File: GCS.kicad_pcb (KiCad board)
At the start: 2 copper layers, 0 parts

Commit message: Added redesigned schematics, missing EEPROM
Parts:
- added C1: 15nF, Capacitor_THT:C_Rect_L7.0mm_W3.5mm_P5.00mm, F.Cu at (104.1, 86.4)
- added C10: 100nF, Capacitor_THT:C_Rect_L7.0mm_W3.5mm_P5.00mm, F.Cu at (97.9, 143.5)
- added C11: 100nF, Capacitor_THT:C_Rect_L7.0mm_W3.5mm_P5.00mm, F.Cu at (54.6, 179.1)
- added C2: 100nF, Capacitor_THT:C_Rect_L7.0mm_W3.5mm_P5.00mm, F.Cu at (110.2, -12.9)
- added C3: 15nF, Capacitor_THT:C_Rect_L7.0mm_W3.5mm_P5.00mm, F.Cu at (104.1, 91.4)
- added C4: 100nF, Capacitor_THT:C_Rect_L7.0mm_W3.5mm_P5.00mm, F.Cu at (101.6, -18.0)
- added C5: 100nF, Capacitor_THT:C_Rect_L7.0mm_W3.5mm_P5.00mm, F.Cu at (110.2, -18.0)
- added C6: 100nF, Capacitor_THT:C_Rect_L7.0mm_W3.5mm_P5.00mm, F.Cu at (118.7, -18.0)
- added C7: 100nF, Capacitor_THT:C_Rect_L7.0mm_W3.5mm_P5.00mm, F.Cu at (101.6, -12.9)
- added C8: 100nF, Capacitor_THT:C_Rect_L7.0mm_W3.5mm_P5.00mm, F.Cu at (87.6, 81.2)
- added C9: 100nF, Capacitor_THT:C_Rect_L7.0mm_W3.5mm_P5.00mm, F.Cu at (63.5, 88.8)
- added J1: Conn_01x02_Male, Connector_PinHeader_1.00mm:PinHeader_1x02_P1.00mm_Vertical, F.Cu at (108.0, 78.7)
- added J2: USB_B, Connector_USB:USB_B_OST_USB-B1HSxx_Horizontal, F.Cu at (33.0, -2.54)
- added J3: Conn_01x04_Male, Connector_PinHeader_1.00mm:PinHeader_1x04_P1.00mm_Vertical, F.Cu at (171.5, -65.6)
- added J4: Conn_02x03_Counter_Clockwise, Connector_PinHeader_1.00mm:PinHeader_2x03_P1.00mm_Vertical, F.Cu at (127.2, -12.2)
- added J5: Conn_01x04_Male, Connector_PinHeader_1.00mm:PinHeader_1x04_P1.00mm_Vertical, F.Cu at (174.8, -65.6)
- added J6: Conn_02x03_Counter_Clockwise, Connector_PinHeader_1.00mm:PinHeader_2x03_P1.00mm_Vertical, F.Cu at (171.5, -59.5)
- added SW1: SW_Push, Button_Switch_THT:SW_PUSH_6mm, F.Cu at (99.1, 80.0)
- added U1: MC6809, Package_DIP:DIP-40_W15.24mm_Socket, F.Cu at (77.5, 85.1)
- added U10: 74HCT00, Package_DIP:DIP-14_W7.62mm_Socket, F.Cu at (48.3, 160.0)
- added U2: DS1813, Package_TO_SOT_THT:TO-92_Inline, F.Cu at (111.8, 97.8)
- added U3: MC68B21, Package_DIP:DIP-40_W15.24mm, F.Cu at (111.9, -70.8)
- added U4: HM62256BLP-7, Package_DIP:DIP-28_W15.24mm_Socket, F.Cu at (73.7, 125.7)
- added U5: 74LS138, Package_DIP:DIP-16_W7.62mm, F.Cu at (94.0, 137.2)
- added U6: 74LS138, Package_DIP:DIP-16_W7.62mm, F.Cu at (160.6, -70.8)
- added U7: 74LS138, Package_DIP:DIP-16_W7.62mm, F.Cu at (149.7, -70.8)
- added U8: MC6850, Package_DIP:DIP-40_W15.24mm, F.Cu at (93.5, -70.8)
- added U9: MC6850, Package_DIP:DIP-40_W15.24mm, F.Cu at (75.1, -70.8)
- added X1: ACO-xxxMHz, Oscillator:Oscillator_DIP-14, F.Cu at (106.7, 114.3)
- added Y1: Crystal, Crystal:Crystal_HC18-U_Vertical, F.Cu at (99.1, 86.4)
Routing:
- net GND: track 0.00 -> 93.3 mm
- net /A15: track 0.00 -> 82.0 mm
- net VCC: track 0.00 -> 72.0 mm
- net /A13: track 0.00 -> 70.4 mm
- net /A14: track 0.00 -> 50.5 mm
- net /~RESET: track 0.00 -> 49.4 mm
- net /D3: track 0.00 -> 44.7 mm
- net /A10: track 0.00 -> 43.4 mm
- net /A11: track 0.00 -> 42.4 mm
- net /D2: track 0.00 -> 35.4 mm
- net /A9: track 0.00 -> 31.3 mm
- net /XTAL: track 0.00 -> 29.5 mm
- net /D1: track 0.00 -> 29.3 mm
- net /EXTAL: track 0.00 -> 26.2 mm
- net /A8: track 0.00 -> 24.7 mm
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
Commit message: Added resistors on async io and changed IC footprints to sockets
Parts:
- added C12: 100nF, Capacitor_THT:C_Rect_L7.0mm_W3.5mm_P5.00mm, F.Cu at (83.4, 86.9)
- added R1: 2.7k, Resistor_THT:R_Axial_DIN0207_L6.3mm_D2.5mm_P7.62mm_Horizontal, F.Cu at (129.5, 23.5)
- added R10: 2.7k, Resistor_THT:R_Axial_DIN0207_L6.3mm_D2.5mm_P7.62mm_Horizontal, F.Cu at (95.8, 73.7)
- added R11: 2.7k, Resistor_THT:R_Axial_DIN0207_L6.3mm_D2.5mm_P7.62mm_Horizontal, F.Cu at (136.8, 31.6)
- added R12: 2.7k, Resistor_THT:R_Axial_DIN0207_L6.3mm_D2.5mm_P7.62mm_Horizontal, F.Cu at (126.0, 35.7)
- added R13: 2.7k, Resistor_THT:R_Axial_DIN0207_L6.3mm_D2.5mm_P7.62mm_Horizontal, F.Cu at (107.6, 58.2)
- added R14: 2.7k, Resistor_THT:R_Axial_DIN0207_L6.3mm_D2.5mm_P7.62mm_Horizontal, F.Cu at (126.0, 39.7)
- added R15: 2.7k, Resistor_THT:R_Axial_DIN0207_L6.3mm_D2.5mm_P7.62mm_Horizontal, F.Cu at (107.6, 54.2)
- added R16: 2.7k, Resistor_THT:R_Axial_DIN0207_L6.3mm_D2.5mm_P7.62mm_Horizontal, F.Cu at (53.5, 87.0)
- added R2: 2.7k, Resistor_THT:R_Axial_DIN0207_L6.3mm_D2.5mm_P7.62mm_Horizontal, F.Cu at (129.5, 27.6)
- added R3: 2.7k, Resistor_THT:R_Axial_DIN0207_L6.3mm_D2.5mm_P7.62mm_Horizontal, F.Cu at (115.2, 31.1)
- added R4: 2.7k, Resistor_THT:R_Axial_DIN0207_L6.3mm_D2.5mm_P7.62mm_Horizontal, F.Cu at (115.2, 35.2)
- added R5: 2.7k, Resistor_THT:R_Axial_DIN0207_L6.3mm_D2.5mm_P7.62mm_Horizontal, F.Cu at (115.2, 39.2)
- added R6: 2.7k, Resistor_THT:R_Axial_DIN0207_L6.3mm_D2.5mm_P7.62mm_Horizontal, F.Cu at (115.2, 43.3)
- added R7: 2.7k, Resistor_THT:R_Axial_DIN0207_L6.3mm_D2.5mm_P7.62mm_Horizontal, F.Cu at (115.2, 47.3)
- added R8: 2.7k, Resistor_THT:R_Axial_DIN0207_L6.3mm_D2.5mm_P7.62mm_Horizontal, F.Cu at (72.4, 86.4)
- added R9: 2.7k, Resistor_THT:R_Axial_DIN0207_L6.3mm_D2.5mm_P7.62mm_Horizontal, F.Cu at (126.0, 31.6)
- added U11: 74HCT00, Package_DIP:DIP-14_W7.62mm_Socket, F.Cu at (96.3, 54.3)
- J3, J5: value Conn_01x04_Male -> Conn_02x03_Counter_Clockwise; footprint Connector_PinHeader_1.00mm:PinHeader_1x04_P1.00mm_Vertical -> Connector_PinHeader_1.00mm:PinHeader_2x03_P1.00mm_Vertical
- J4, J6: value Conn_02x03_Counter_Clockwise -> Conn_01x04_Male; footprint Connector_PinHeader_1.00mm:PinHeader_2x03_P1.00mm_Vertical -> Connector_PinHeader_1.00mm:PinHeader_1x04_P1.00mm_Vertical
- U10: value 74HCT00 -> MC6850; footprint Package_DIP:DIP-14_W7.62mm_Socket -> Package_DIP:DIP-40_W15.24mm_Socket
- U3: footprint Package_DIP:DIP-40_W15.24mm -> Package_DIP:DIP-40_W15.24mm_Socket
- U5: value 74LS138 -> 29C256; footprint Package_DIP:DIP-16_W7.62mm -> Package_DIP:DIP-28_W15.24mm_Socket
- U6, U7: footprint Package_DIP:DIP-16_W7.62mm -> Package_DIP:DIP-16_W7.62mm_Socket
- U8: footprint Package_DIP:DIP-40_W15.24mm -> Package_DIP:DIP-24_W15.24mm_Socket
- U9: value MC6850 -> 74LS138; footprint Package_DIP:DIP-40_W15.24mm -> Package_DIP:DIP-16_W7.62mm_Socket
- X1: value ACO-xxxMHz -> CXO_DIP8; footprint Oscillator:Oscillator_DIP-14 -> Oscillator:Oscillator_DIP-8
- moved U7 184.1 mm to (30.5, 69.5)
- moved C11 184.1 mm to (142.6, 17.4), turned to 0 degrees
- moved U6 183.6 mm to (42.2, 69.5)
- moved J6 167.0 mm to (72.5, 74.9)
- moved J5 160.1 mm to (104.5, 78.2)
- moved U9 151.2 mm to (18.7, 69.5)
- moved U10 143.4 mm to (38.1, 17.0)
- moved U3 128.0 mm to (18.7, 17.0)
- moved U8 126.2 mm to (76.9, 54.3)
- moved U5 121.4 mm to (76.9, 17.0), turned to 0 degrees
- moved U4 111.1 mm to (96.3, 17.0), turned to 0 degrees
- moved J3 104.1 mm to (145.4, 35.2)
- moved C10 103.2 mm to (126.2, 44.3), turned to 0 degrees
- moved C5 102.2 mm to (96.0, 83.3)
- moved J4 97.8 mm to (72.5, 68.9)
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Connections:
- J2 pad 2: Net-(J2-Pad2) -> (no net)
- J2 pad 3: Net-(J2-Pad3) -> (no net)
- J3 pad 1: GND -> Net-(J3-Pad1)
- J3 pad 2: /TX0 -> Net-(J3-Pad2)
- J3 pad 3: /RX0 -> Net-(J3-Pad3)
- J3 pad 4: VCC -> GND
- J4 pad 1: /~DCD0 -> GND
- J4 pad 2: /~CTS0 -> Net-(J4-Pad2)
- J4 pad 3: /~RTS0 -> Net-(J4-Pad3)
- J4 pad 4: GND -> VCC
- J5 pad 1: GND -> Net-(J5-Pad1)
- J5 pad 2: /TX1 -> Net-(J5-Pad2)
- J5 pad 3: /RX1 -> Net-(J5-Pad3)
- J5 pad 4: VCC -> GND
- J6 pad 1: /~DCD1 -> GND
- J6 pad 2: /~CTS1 -> Net-(J6-Pad2)
- J6 pad 3: /~RTS1 -> Net-(J6-Pad3)
- J6 pad 4: GND -> VCC
- U1 pad 2: Net-(U1-Pad2) -> (no net)
- U1 pad 3: Net-(U1-Pad3) -> /~IRQ
- U1 pad 33: VCC -> Net-(R1-Pad2)
- U1 pad 35: Net-(U1-Pad35) -> (no net)
- U1 pad 36: VCC -> Net-(R1-Pad2)
- U1 pad 4: Net-(U1-Pad4) -> (no net)
- U1 pad 40: VCC -> Net-(R1-Pad2)
- U1 pad 5: Net-(U1-Pad5) -> (no net)
- U1 pad 6: Net-(U1-Pad6) -> (no net)
- U10 pad 1: /E -> GND
- U10 pad 10: /~R~W -> Net-(R11-Pad1)
- U10 pad 11: /BRAM -> /A0
- U10 pad 12: /~BRAM0 -> VCC
- U10 pad 13: /~BRAM1 -> /R~W
- U10 pad 14: VCC -> /E
- U10 pad 2: /R~W -> /RX1
- U10 pad 3: /~R -> /E
- U10 pad 4: /R~W -> /E
- U10 pad 5: /R~W -> /~RTS1
- U10 pad 6: /~R~W -> /TX1
- U10 pad 7: GND -> /~IRQ
- U10 pad 8: /~W -> Net-(R11-Pad1)
- U10 pad 9: /E -> /~ASYNC1_E
- U3 pad 10: Net-(U3-Pad10) -> (no net)
- U3 pad 11: Net-(U3-Pad11) -> (no net)
- U3 pad 12: Net-(U3-Pad12) -> (no net)
- U3 pad 13: Net-(U3-Pad13) -> (no net)
- U3 pad 14: Net-(U3-Pad14) -> (no net)
- U3 pad 15: Net-(U3-Pad15) -> (no net)
- U3 pad 16: Net-(U3-Pad16) -> (no net)
- U3 pad 17: Net-(U3-Pad17) -> (no net)
- U3 pad 18: Net-(U3-Pad18) -> (no net)
- U3 pad 19: Net-(U3-Pad19) -> (no net)
- U3 pad 2: Net-(U3-Pad2) -> (no net)
- U3 pad 22: VCC -> Net-(R2-Pad1)
- U3 pad 24: VCC -> Net-(R2-Pad1)
- U3 pad 3: Net-(U3-Pad3) -> (no net)
- U3 pad 37: Net-(U3-Pad37) -> /~IRQ
- U3 pad 38: Net-(U3-Pad38) -> /~IRQ
- U3 pad 39: Net-(U3-Pad39) -> (no net)
- U3 pad 4: Net-(U3-Pad4) -> (no net)
- U3 pad 40: Net-(U3-Pad40) -> (no net)
- U3 pad 5: Net-(U3-Pad5) -> (no net)
- U3 pad 6: Net-(U3-Pad6) -> (no net)
- U3 pad 7: Net-(U3-Pad7) -> (no net)
- U3 pad 8: Net-(U3-Pad8) -> (no net)
- U3 pad 9: Net-(U3-Pad9) -> (no net)
- U5 pad 1: /A13 -> /~W
- U5 pad 10: /~BRAM1 -> /A0
- U5 pad 11: /~BRAM0 -> /D0
- U5 pad 12: Net-(U5-Pad12) -> /D1
- U5 pad 13: Net-(U5-Pad13) -> /D2
- U5 pad 14: Net-(U5-Pad14) -> GND
- U5 pad 15: Net-(U5-Pad15) -> /D3
- U5 pad 16: VCC -> /D4
- U5 pad 2: /A14 -> /A12
- U5 pad 3: /A15 -> /A7
- U5 pad 4: GND -> /A6
- U5 pad 5: GND -> /A5
- U5 pad 6: /A15 -> /A4
- U5 pad 7: /~ROM -> /A3
- U5 pad 8: GND -> /A2
- U5 pad 9: /~IO -> /A1
- U6 pad 1: /A10 -> /A13
- U6 pad 10: /~IO5 -> /~BRAM1
- U6 pad 11: /~IO4 -> /~BRAM0
- U6 pad 12: /~IO3 -> (no net)
- U6 pad 13: /~IO2 -> (no net)
- U6 pad 14: /~IO1 -> (no net)
- U6 pad 15: /~INT_IO -> (no net)
- U6 pad 2: /A11 -> /A14
- U6 pad 3: /A12 -> /A15
- U6 pad 5: /~IO -> GND
- U6 pad 6: VCC -> /A15
- U6 pad 7: /~IO7 -> /~ROM
- U6 pad 9: /~IO6 -> /~IO
- U7 pad 1: /A4 -> /A10
- U7 pad 10: Net-(U7-Pad10) -> (no net)
- U7 pad 11: /~VDP_E -> (no net)
- U7 pad 12: /~ASYNC1_E -> (no net)
- U7 pad 13: /~ASYNC0_E -> (no net)
- U7 pad 14: /~PIA_E -> (no net)
- U7 pad 15: /~CFLASH_E -> /~INT_IO
- U7 pad 2: /A5 -> /A11
- U7 pad 3: /A6 -> /A12
- U7 pad 5: /~INT_IO -> /~IO
- U7 pad 6: VCC -> Net-(R3-Pad1)
- U7 pad 7: Net-(U7-Pad7) -> (no net)
- U7 pad 9: Net-(U7-Pad9) -> (no net)
- U8 pad 10: VCC -> Net-(R4-Pad1)
- U8 pad 15: Net-(U8-Pad15) -> (no net)
- U8 pad 16: Net-(U8-Pad16) -> (no net)
- U8 pad 17: Net-(U8-Pad17) -> (no net)
- U8 pad 18: Net-(U8-Pad18) -> (no net)
- U8 pad 19: Net-(U8-Pad19) -> (no net)
- U8 pad 20: Net-(U8-Pad20) -> (no net)
- U8 pad 21: Net-(U8-Pad21) -> (no net)
- U8 pad 22: Net-(U8-Pad22) -> (no net)
- U8 pad 7: Net-(U8-Pad7) -> /~IRQ
- U8 pad 8: VCC -> Net-(R4-Pad1)
- U9 pad 1: GND -> /A4
- U9 pad 10: VCC -> (no net)
- U9 pad 11: /A0 -> (no net)
- U9 pad 12: VCC -> /~ASYNC1_E
- U9 pad 13: /R~W -> /~ASYNC0_E
- U9 pad 14: /E -> /~PIA_E
- U9 pad 15: Net-(U9-Pad15) -> (no net)
- U9 pad 16: Net-(U9-Pad16) -> VCC
- U9 pad 2: /RX1 -> /A5
- U9 pad 3: /E -> /A6
- U9 pad 4: /E -> GND
- U9 pad 5: /~RTS1 -> /~INT_IO
- U9 pad 6: /TX1 -> Net-(R5-Pad1)
- U9 pad 7: Net-(U9-Pad7) -> (no net)
- U9 pad 8: VCC -> GND
- U9 pad 9: /~ASYNC1_E -> (no net)
- X1 pad 1: Net-(X1-Pad1) -> (no net)
- X1 pad 8: /XTAL -> VCC
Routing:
- net GND: track 93.3 -> 0.00 mm
- net /A15: track 82.0 -> 0.00 mm
- net VCC: track 72.0 -> 0.00 mm
- net /A13: track 70.4 -> 0.00 mm
- net /A14: track 50.5 -> 0.00 mm
- net /~RESET: track 49.4 -> 0.00 mm
- net /D3: track 44.7 -> 0.00 mm
- net /A10: track 43.4 -> 0.00 mm
- net /A11: track 42.4 -> 0.00 mm
- net /D2: track 35.4 -> 0.00 mm
- net /A9: track 31.3 -> 0.00 mm
- net /XTAL: track 29.5 -> 0.00 mm
- net /D1: track 29.3 -> 0.00 mm
- net /EXTAL: track 26.2 -> 0.00 mm
- net /A8: track 24.7 -> 0.00 mm
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
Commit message: Began rerouting PCB
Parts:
- added J7: ASYNC1_OPT, Connector_PinHeader_2.54mm:PinHeader_2x03_P2.54mm_Vertical, F.Cu at (443.0, 136.7)
- added J8: ASYNC1_IO, Connector_PinHeader_2.54mm:PinHeader_1x04_P2.54mm_Vertical, F.Cu at (419.0, 135.3)
- added R17: 2.7k, Resistor_THT:R_Axial_DIN0207_L6.3mm_D2.5mm_P7.62mm_Horizontal, F.Cu at (428.4, 146.8)
- added R18: 2.7k, Resistor_THT:R_Axial_DIN0207_L6.3mm_D2.5mm_P7.62mm_Horizontal, F.Cu at (404.7, 134.6)
- added R19: 2.7k, Resistor_THT:R_Axial_DIN0207_L6.3mm_D2.5mm_P7.62mm_Horizontal, F.Cu at (404.9, 141.4)
- J1: value Conn_01x02_Male -> PROC_EXTAL_GND; footprint Connector_PinHeader_1.00mm:PinHeader_1x02_P1.00mm_Vertical -> Connector_PinHeader_2.54mm:PinHeader_1x02_P2.54mm_Vertical
- J3: value Conn_02x03_Counter_Clockwise -> PA_CON; footprint Connector_PinHeader_1.00mm:PinHeader_2x03_P1.00mm_Vertical -> Connector_PinSocket_2.54mm:PinSocket_1x10_P2.54mm_Vertical
- J4: value Conn_01x04_Male -> PB_CON; footprint Connector_PinHeader_1.00mm:PinHeader_1x04_P1.00mm_Vertical -> Connector_PinSocket_2.54mm:PinSocket_1x10_P2.54mm_Vertical
- J5: value Conn_02x03_Counter_Clockwise -> ASYNC0_OPT; footprint Connector_PinHeader_1.00mm:PinHeader_2x03_P1.00mm_Vertical -> Connector_PinHeader_2.54mm:PinHeader_2x03_P2.54mm_Vertical
- J6: value Conn_01x04_Male -> ASYNC0_IO; footprint Connector_PinHeader_1.00mm:PinHeader_1x04_P1.00mm_Vertical -> Connector_PinHeader_2.54mm:PinHeader_1x04_P2.54mm_Vertical
- U10: footprint Package_DIP:DIP-40_W15.24mm_Socket -> Package_DIP:DIP-24_W15.24mm_Socket
- moved U10 390.1 mm to (420.0, 96.6)
- moved R16 378.5 mm to (428.2, 139.9)
- moved R15 330.7 mm to (428.6, 133.3)
- moved C10 302.9 mm to (425.7, 89.6)
- moved U9 294.5 mm to (298.0, -23.9)
- moved R14 293.8 mm to (407.8, 122.9)
- moved J6 285.0 mm to (351.7, 132.2)
- moved U8 277.1 mm to (350.9, 96.1)
- moved J5 275.2 mm to (373.7, 135.4)
- moved R10 271.5 mm to (359.5, 138.4)
- moved J2 260.9 mm to (225.8, -122.2)
- moved R9 253.9 mm to (359.4, 131.5)
- moved U7 253.5 mm to (264.9, -27.0)
- moved R11 249.7 mm to (359.3, 145.0)
- moved R13 245.5 mm to (339.6, 138.5)
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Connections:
- J3 pad 4: GND -> Net-(J3-Pad4)
- J3 pad 5: GND -> Net-(J3-Pad5)
- J3 pad 6: GND -> Net-(J3-Pad6)
- J4 pad 1: GND -> Net-(J4-Pad1)
- J4 pad 4: VCC -> Net-(J4-Pad4)
- J5 pad 2: Net-(J5-Pad2) -> GND
- J5 pad 5: GND -> Net-(J5-Pad5)
- R10 pad 1: Net-(J4-Pad2) -> Net-(J5-Pad3)
- R10 pad 2: /TX0 -> /~CTS0
- R11 pad 1: Net-(R11-Pad1) -> Net-(J5-Pad5)
- R11 pad 2: VCC -> /~RTS0
- R12 pad 1: Net-(J5-Pad1) -> Net-(J6-Pad3)
- R12 pad 2: /~DCD1 -> /RX0
- R13 pad 1: Net-(J5-Pad2) -> Net-(J6-Pad2)
- R13 pad 2: /~CTS1 -> /TX0
- R14 pad 1: Net-(J5-Pad3) -> Net-(R14-Pad1)
- R14 pad 2: /~RTS1 -> VCC
- R15 pad 1: Net-(J6-Pad3) -> Net-(J7-Pad1)
- R15 pad 2: /RX1 -> /~DCD1
- R16 pad 1: Net-(J6-Pad2) -> Net-(J7-Pad3)
- R16 pad 2: /TX1 -> /~CTS1
- R2 pad 1: Net-(R2-Pad1) -> VCC
- R2 pad 2: VCC -> /~FIRQ
- R3 pad 1: Net-(R3-Pad1) -> VCC
- R3 pad 2: VCC -> /~IRQ
- R4 pad 1: Net-(R4-Pad1) -> VCC
- R4 pad 2: VCC -> /~NMI
- R6 pad 1: Net-(J3-Pad1) -> Net-(R6-Pad1)
- R6 pad 2: /~DCD0 -> VCC
- R7 pad 1: Net-(J3-Pad2) -> Net-(R7-Pad1)
- R7 pad 2: /~CTS0 -> VCC
- R8 pad 1: Net-(J3-Pad3) -> Net-(R8-Pad1)
- R8 pad 2: /~RTS0 -> VCC
- R9 pad 1: Net-(J4-Pad3) -> Net-(J5-Pad1)
- R9 pad 2: /RX0 -> /~DCD0
- U1 pad 2: (no net) -> /~NMI
- U1 pad 4: (no net) -> /~FIRQ
- U10 pad 10: Net-(R11-Pad1) -> Net-(R14-Pad1)
- U10 pad 8: Net-(R11-Pad1) -> Net-(R14-Pad1)
- U11 pad 10: /~R~W -> /R~W
- U11 pad 4: /R~W -> /E
- U11 pad 5: /R~W -> /~R~W
- U11 pad 6: /~R~W -> /~W
- U11 pad 8: /~W -> /~R~W
- U11 pad 9: /E -> /R~W
- U3 pad 10: (no net) -> Net-(J4-Pad1)
- U3 pad 11: (no net) -> Net-(J4-Pad2)
- U3 pad 12: (no net) -> Net-(J4-Pad3)
- U3 pad 13: (no net) -> Net-(J4-Pad4)
- U3 pad 14: (no net) -> Net-(J4-Pad5)
- U3 pad 15: (no net) -> Net-(J4-Pad6)
- U3 pad 16: (no net) -> Net-(J4-Pad7)
- U3 pad 17: (no net) -> Net-(J4-Pad8)
- U3 pad 18: (no net) -> Net-(J4-Pad9)
- U3 pad 19: (no net) -> Net-(J4-Pad10)
- U3 pad 2: (no net) -> Net-(J3-Pad1)
- U3 pad 22: Net-(R2-Pad1) -> Net-(R5-Pad1)
- U3 pad 24: Net-(R2-Pad1) -> Net-(R5-Pad1)
- U3 pad 3: (no net) -> Net-(J3-Pad2)
- U3 pad 39: (no net) -> Net-(J3-Pad10)
- U3 pad 4: (no net) -> Net-(J3-Pad3)
- U3 pad 40: (no net) -> Net-(J3-Pad9)
- U3 pad 5: (no net) -> Net-(J3-Pad4)
- U3 pad 6: (no net) -> Net-(J3-Pad5)
- U3 pad 7: (no net) -> Net-(J3-Pad6)
- U3 pad 8: (no net) -> Net-(J3-Pad7)
- U3 pad 9: (no net) -> Net-(J3-Pad8)
- U7 pad 6: Net-(R3-Pad1) -> Net-(R6-Pad1)
- U8 pad 10: Net-(R4-Pad1) -> Net-(R7-Pad1)
- U8 pad 8: Net-(R4-Pad1) -> Net-(R7-Pad1)
- U9 pad 6: Net-(R5-Pad1) -> Net-(R8-Pad1)
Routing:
- net VCC: track 0.00 -> 101.8 mm
- net GND: track 0.00 -> 70.0 mm
- net Net-(R1-Pad2): track 0.00 -> 39.7 mm
- net /R~W: track 0.00 -> 33.8 mm
- net /~RESET: track 0.00 -> 29.7 mm
- net /E: track 0.00 -> 28.8 mm
- net /XTAL: track 0.00 -> 28.6 mm
- net /EXTAL: track 0.00 -> 14.9 mm
- net /~R~W: track 0.00 -> 9.72 mm
- net /~NMI: track 0.00 -> 3.30 mm
- net /~FIRQ: track 0.00 -> 3.30 mm
- net /~IRQ: track 0.00 -> 2.98 mm
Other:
- net class Default: clearance 0.2 -> 0.127; trace_width 0.25 -> 0.127; via_dia 0.8 -> 0.6; via_drill 0.4 -> 0.3
- rule trace_clearance: 0.2 -> 0.127
- rule trace_min: 0.2 -> 0.127
- rule via_min_size: 0.4 -> 0.6

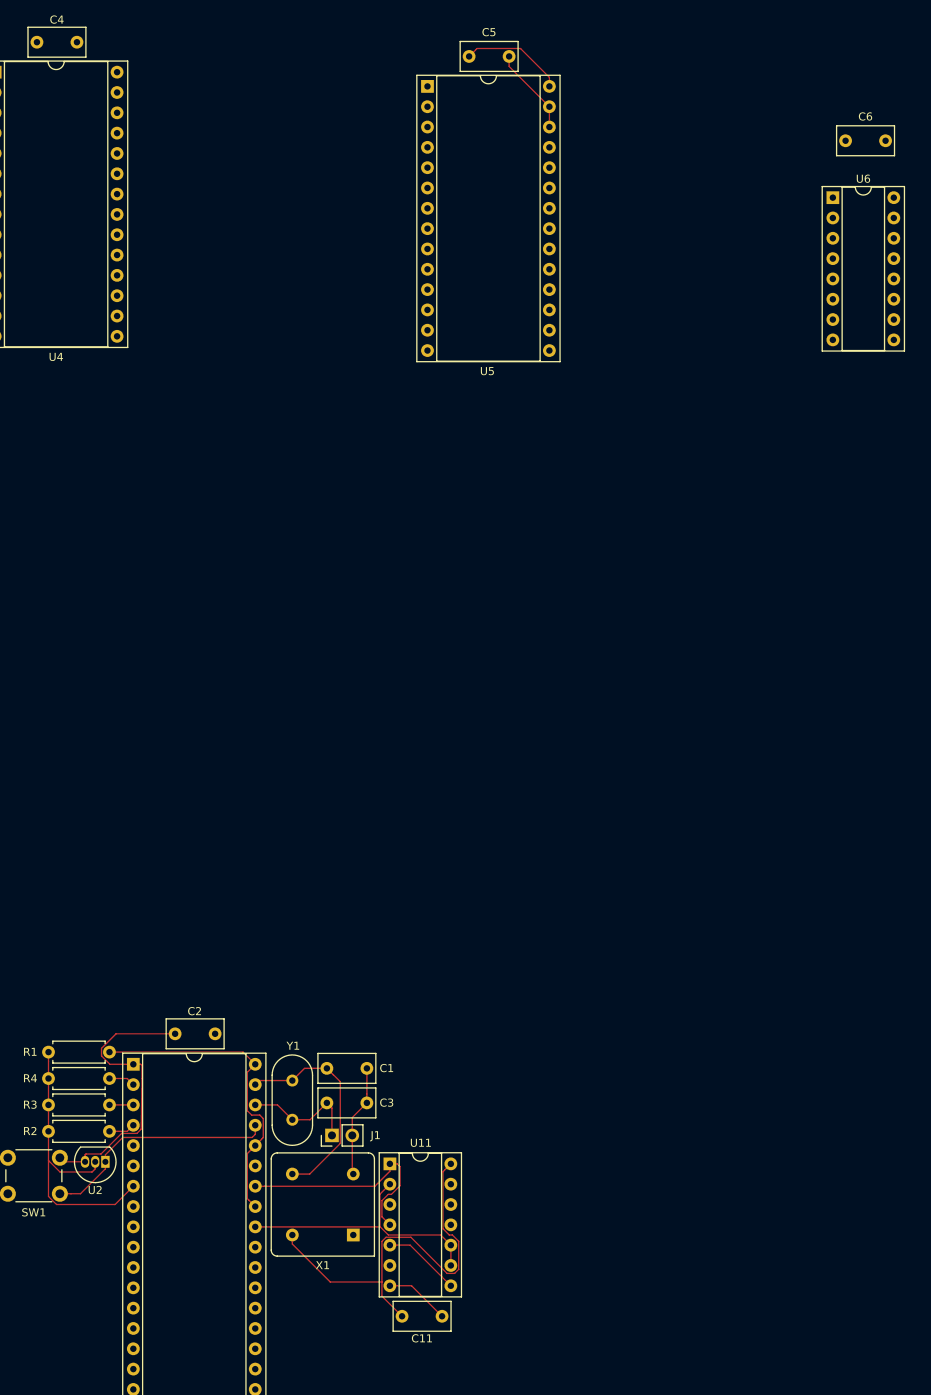
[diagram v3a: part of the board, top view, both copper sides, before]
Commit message: Combined footprint of crystal and oscillator
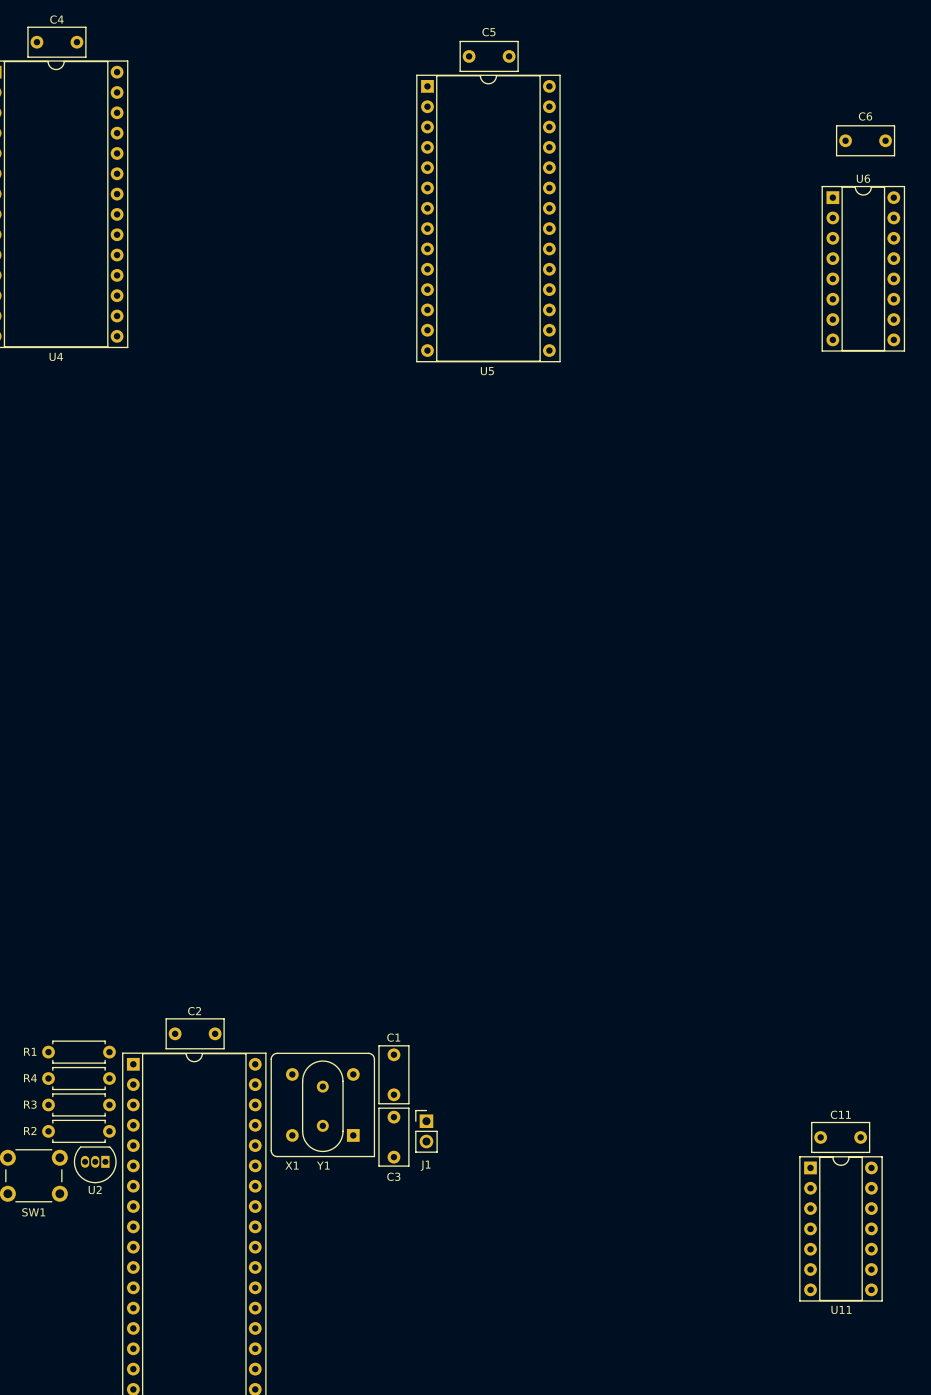
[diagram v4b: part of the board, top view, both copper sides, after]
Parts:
- moved C11 56.9 mm to (226.3, 89.4)
- moved U11 52.6 mm to (225.0, 93.2)
- moved X1 12.4 mm to (167.9, 89.2)
- moved J1 11.9 mm to (177.0, 87.4), turned to 0 degrees
- moved C1 9.01 mm to (173.0, 84.1), turned to 90 degrees
- moved C3 8.57 mm to (173.0, 86.9), turned to 270 degrees
- moved Y1 3.89 mm to (164.1, 83.1)
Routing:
- net VCC: track 101.8 -> 0.00 mm
- net GND: track 70.0 -> 0.00 mm
- net Net-(R1-Pad2): track 39.7 -> 0.00 mm
- net /R~W: track 33.8 -> 0.00 mm
- net /~RESET: track 29.7 -> 0.00 mm
- net /E: track 28.8 -> 0.00 mm
- net /XTAL: track 28.6 -> 0.00 mm
- net /EXTAL: track 14.9 -> 0.00 mm
- net /~R~W: track 9.72 -> 0.00 mm
- net /~NMI: track 3.30 -> 0.00 mm
- net /~FIRQ: track 3.30 -> 0.00 mm
- net /~IRQ: track 2.98 -> 0.00 mm

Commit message: Routed first decoder
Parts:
- moved C5 194.5 mm to (91.4, 126.2), turned to 180 degrees
- moved C6 190.3 mm to (159.3, 141.7), turned to 90 degrees
- moved U5 183.1 mm to (96.5, 122.4), turned to 180 degrees
- moved U6 178.8 mm to (155.4, 135.4), turned to 270 degrees
- moved C4 175.5 mm to (108.5, 126.2), turned to 0 degrees
- moved U4 166.3 mm to (118.1, 122.4), turned to 180 degrees
- moved R6 109.5 mm to (349.5, 37.4)
- moved C7 109.5 mm to (363.0, 17.7)
- moved U7 109.5 mm to (361.4, 24.8)
- moved U11 66.1 mm to (159.3, 99.8)
- moved C11 61.1 mm to (165.6, 96.0), turned to 180 degrees
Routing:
- net GND: track 0.00 -> 320.6 mm
- net VCC: track 0.00 -> 169.7 mm
- net /~W: track 0.00 -> 98.2 mm
- net /A15: track 0.00 -> 92.0 mm
- net /D6: track 0.00 -> 91.7 mm
- net /D7: track 0.00 -> 91.0 mm
- net /A10: track 0.00 -> 89.5 mm
- net /D5: track 0.00 -> 86.1 mm
- net /D4: track 0.00 -> 85.3 mm
- net /D3: track 0.00 -> 85.3 mm
- net /~ROM: track 0.00 -> 83.9 mm
- net /A11: track 0.00 -> 78.3 mm
- net /D2: track 0.00 -> 72.8 mm
- net /A9: track 0.00 -> 70.5 mm
- net /A13: track 0.00 -> 70.0 mm
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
